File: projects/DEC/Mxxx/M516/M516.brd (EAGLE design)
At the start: 125.7 x 62.2 mm, 45 parts

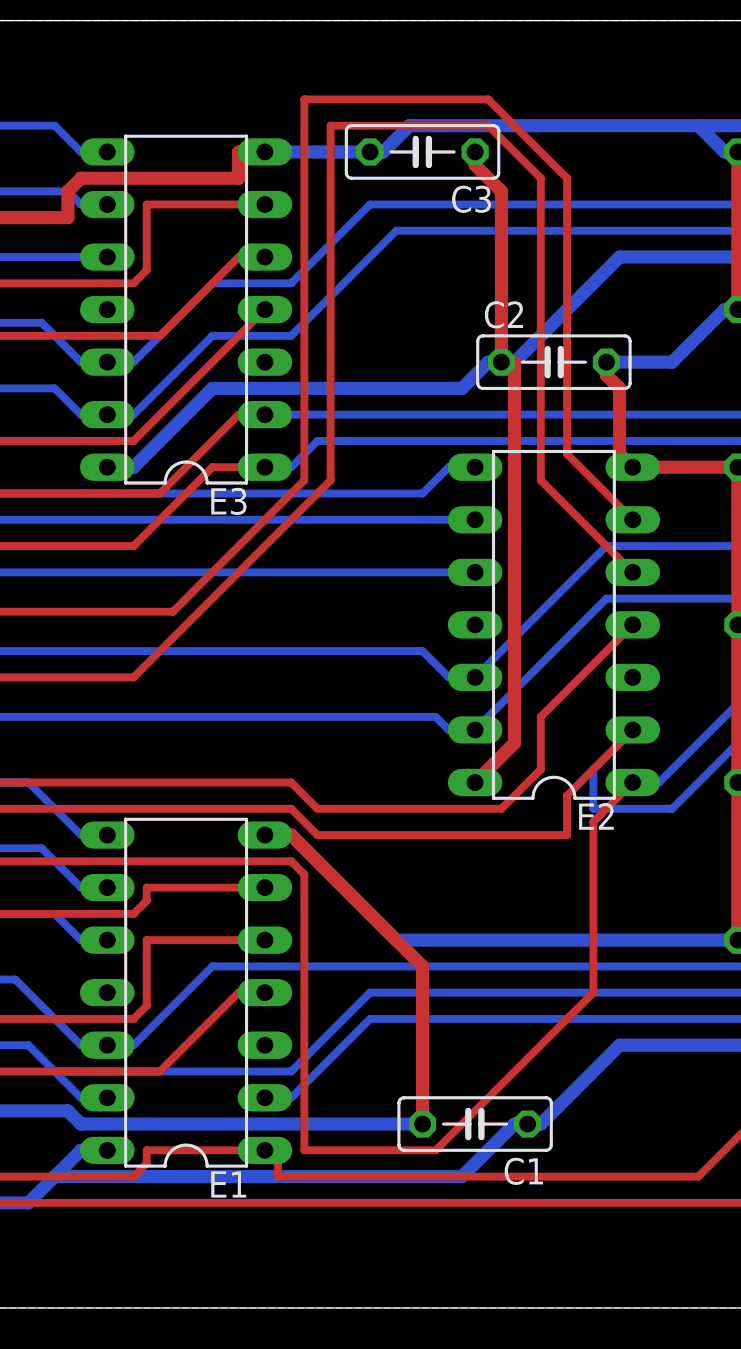
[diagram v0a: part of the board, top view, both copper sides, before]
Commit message: Where possible, map 74xx-jameco to 74xx-us. Moved the 7438 to dec-con.lbr. Also changed the spelling of CRYTAL to CRYSTAL.
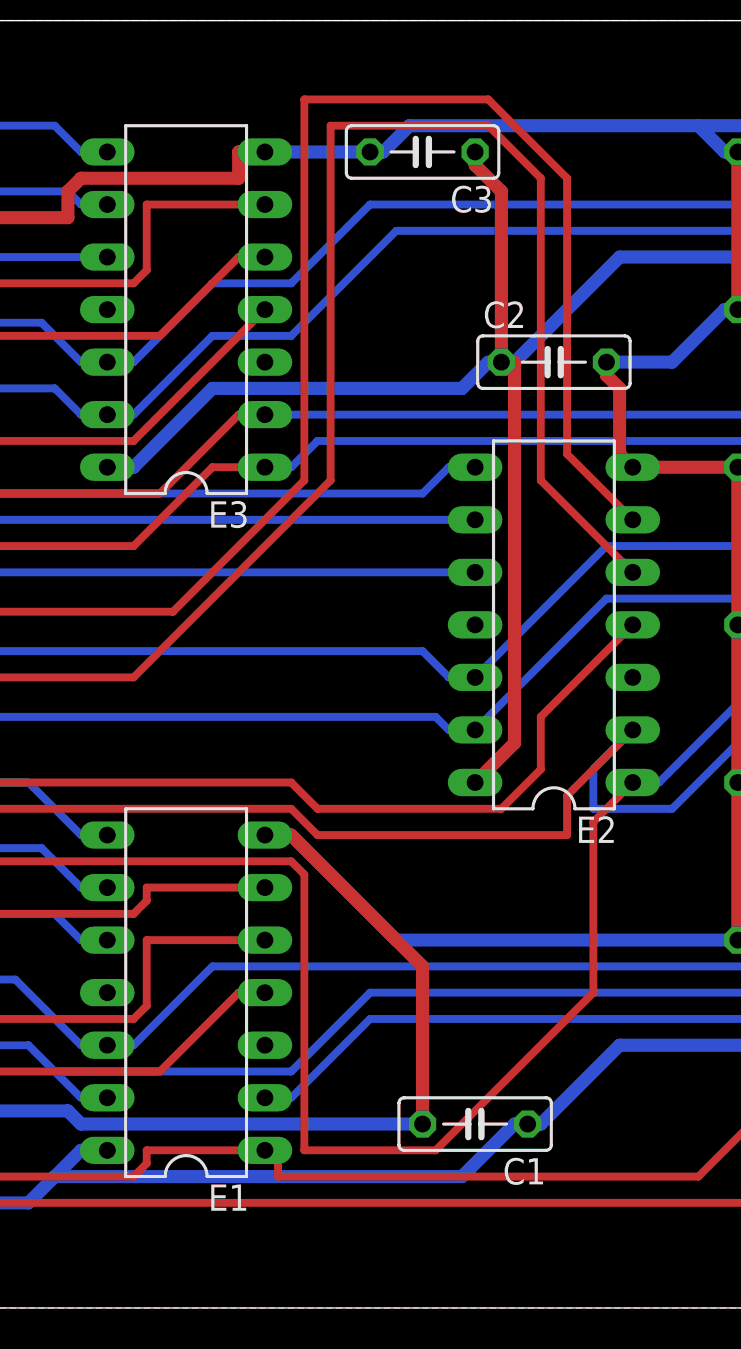
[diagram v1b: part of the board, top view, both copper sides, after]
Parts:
- E1, E2, E3: value (none) -> 74S20N; device 74xx-jameco:DIL14 -> 74xx-us:DIL14
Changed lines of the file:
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@@
 <element name="U$1" library="dec-con" package="SINGLE" value="OUTLINE-SINGLE" x="0" y="0"/>
 <element name="U$2" library="dec-con" package="EDGE-CON2" value="" x="0" y="0"/>
-<element name="E1" library="74xx-jameco" package="DIL14" value="" x="29.21" y="15.24" rot="R90"/>
+<element name="E1" library="74xx-us" package="DIL14" value="74S20N" x="29.21" y="15.24" rot="R90"/>
 <element name="R1" library="rcl" package="0207/10" value="220" x="68.58" y="13.97"/>
 <element name="R2" library="rcl" package="0207/10" value="750" x="73.66" y="17.78"/>
@@
 <element name="D3" library="diode" package="DO35-10" value="D664" x="86.36" y="21.59" rot="R180"/>
 <element name="D4" library="diode" package="DO35-10" value="D664" x="86.36" y="25.4" rot="R180"/>
-<element name="E2" library="74xx-jameco" package="DIL14" value="" x="46.99" y="33.02" rot="R90"/>
+<element name="E2" library="74xx-us" package="DIL14" value="74S20N" x="46.99" y="33.02" rot="R90"/>
 <element name="R7" library="rcl" package="0207/10" value="220" x="68.58" y="29.21"/>
 <element name="R8" library="rcl" package="0207/10" value="750" x="73.66" y="33.02"/>
@@
 <element name="D7" library="diode" package="DO35-10" value="D664" x="86.36" y="36.83" rot="R180"/>
 <element name="D8" library="diode" package="DO35-10" value="D664" x="86.36" y="40.64" rot="R180"/>
-<element name="E3" library="74xx-jameco" package="DIL14" value="" x="29.21" y="48.26" rot="R90"/>
+<element name="E3" library="74xx-us" package="DIL14" value="74S20N" x="29.21" y="48.26" rot="R90"/>
 <element name="R13" library="rcl" package="0207/10" value="220" x="68.58" y="44.45"/>
 <element name="R14" library="rcl" package="0207/10" value="750" x="73.66" y="48.26"/>

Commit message: Walk the project tree, making things pass current design rules.
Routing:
- net A1: track 127.2 -> 90.2 mm
- net M1: track 122.7 -> 86.2 mm
- net K1: track 81.5 -> 45.6 mm
- net L1: track 80.2 -> 45.1 mm
- net VCC: track 245.8 -> 263.3 mm
- net F1: track 90.3 -> 77.6 mm
- net B1: track 67.2 -> 77.6 mm
- net H1: track 98.6 -> 89.4 mm
- net +3.2V: track 66.8 -> 60.9 mm
- net GND: track 265.0 -> 260.2 mm
- net J1: track 48.6 -> 45.6 mm
- net N1: track 88.2 -> 90.5 mm
- net K2: track 90.2 -> 92.0 mm
- net D1: track 28.5 -> 26.8 mm
- net S1: track 28.6 -> 27.1 mm
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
